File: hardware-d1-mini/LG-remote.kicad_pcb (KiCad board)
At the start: 2 copper layers, 46.4 x 26.9 mm, 11 parts, among them J1 Screw_Terminal_01x03, U1 TSR_1-2412, U2 MCP2021A-xxxxSN, U3 WeMos_D1_mini

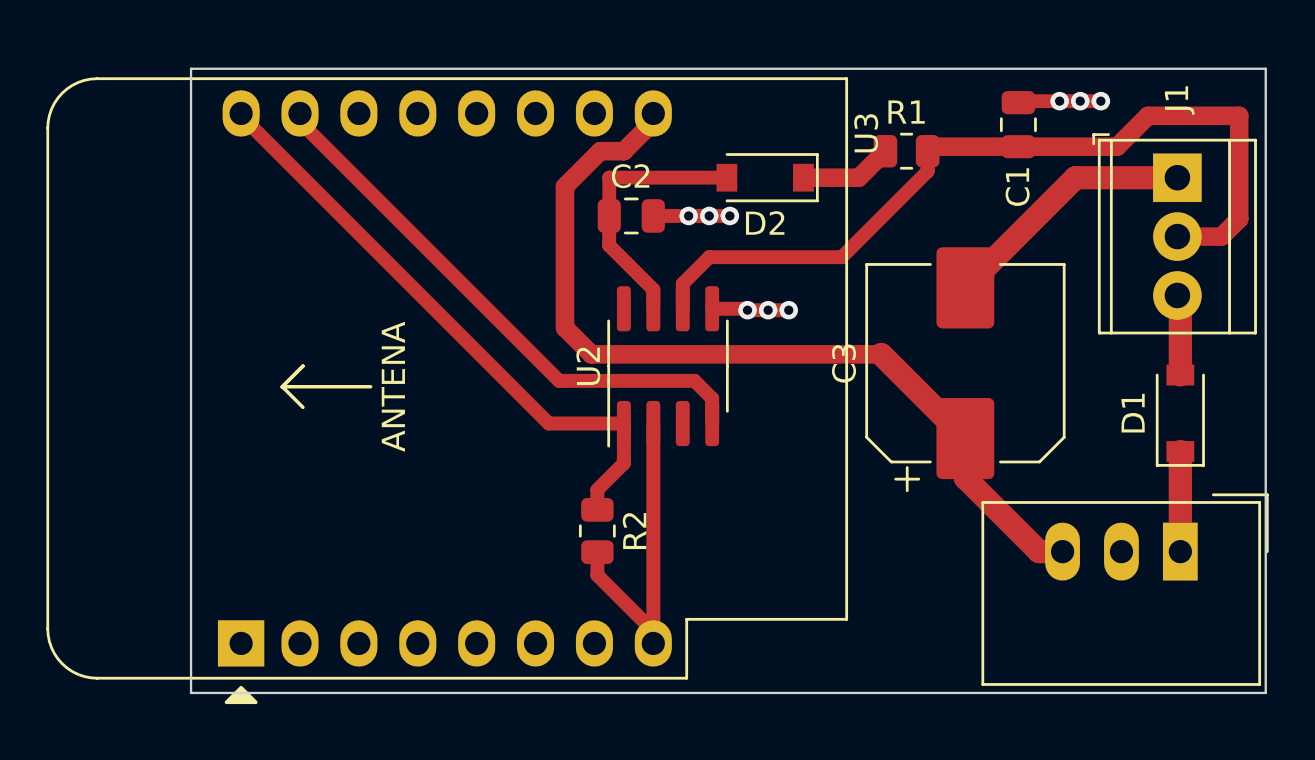
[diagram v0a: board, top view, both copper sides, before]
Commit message: 12v line fix
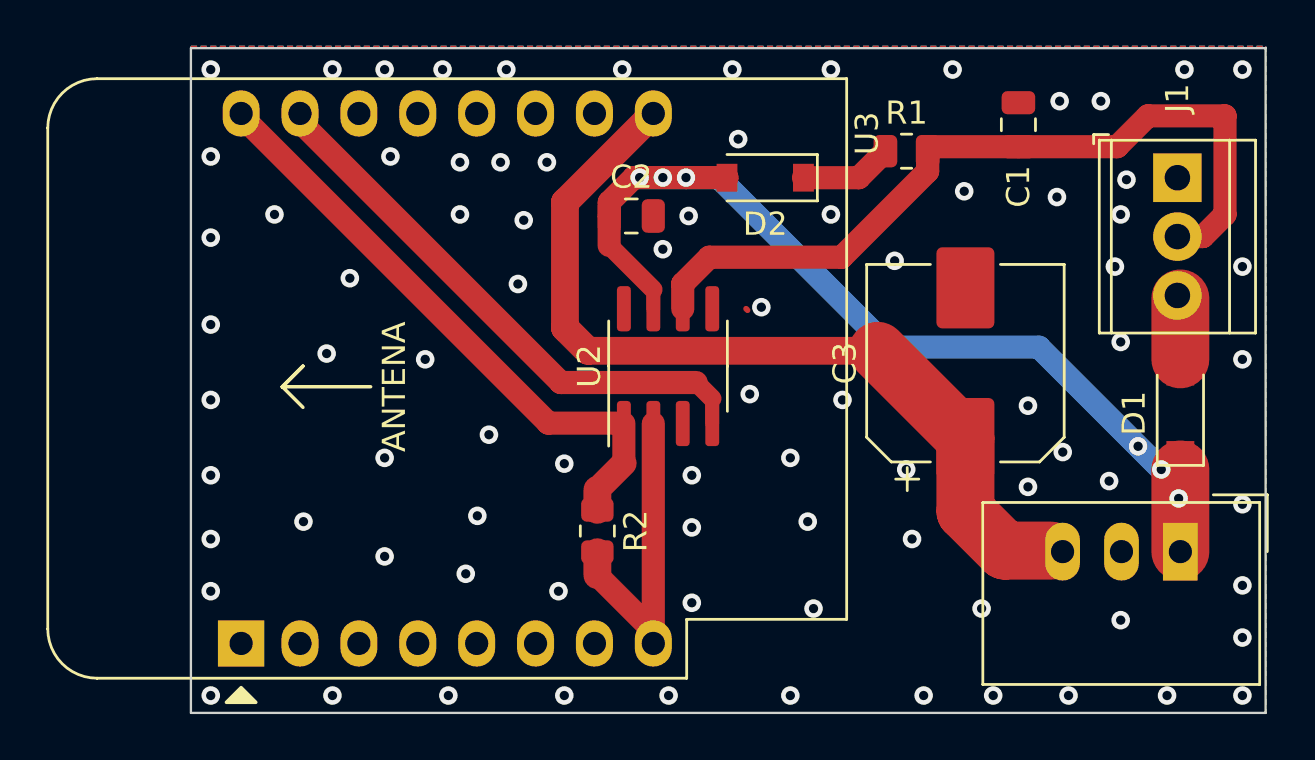
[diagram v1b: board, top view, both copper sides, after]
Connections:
- C2 pad 1: Net-(C2-Pad1) -> +12V
- D1 pad 2: Net-(D1-Pad2) -> +12V
- D2 pad 2: Net-(C2-Pad1) -> +12V
- J1 pad 3: Net-(D1-Pad2) -> +12V
- U2 pad 7: Net-(C2-Pad1) -> +12V
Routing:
- net +12V: track 4.32 -> 47.3 mm, vias 0 -> 6
- net GND: track 21.4 -> 0.09 mm, vias 9 -> 83
- net Net-(C2-Pad1): track 11.5 -> 0.00 mm
- net Net-(D1-Pad2): track 3.48 -> 0.00 mm
- net /LIN: track 36.0 -> 34.7 mm
- added copper zone on F.Cu, net GND
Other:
- board size 46.4 x 26.9 mm -> 46.4 x 28.7 mm
